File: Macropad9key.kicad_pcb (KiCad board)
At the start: 2 copper layers, 75 parts, among them J1 3220-10-0100-00, J2 4POS_2MM, J3 USB4085-GF-A, SW1 CherryMX_WithPCBPins, SW2 CherryMX_WithPCBPins, SW3 CherryMX_WithPCBPins, SW4 CherryMX_WithPCBPins, SW5 CherryMX_WithPCBPins, SW6 CherryMX_WithPCBPins, SW7 CherryMX_WithPCBPins, SW8 CherryMX_WithPCBPins, SW9 CherryMX_WithPCBPins, U1 ATSAMD11D14A-MUT, U2 MCP1700T-3302E-TT, U3 PCA9632DP2

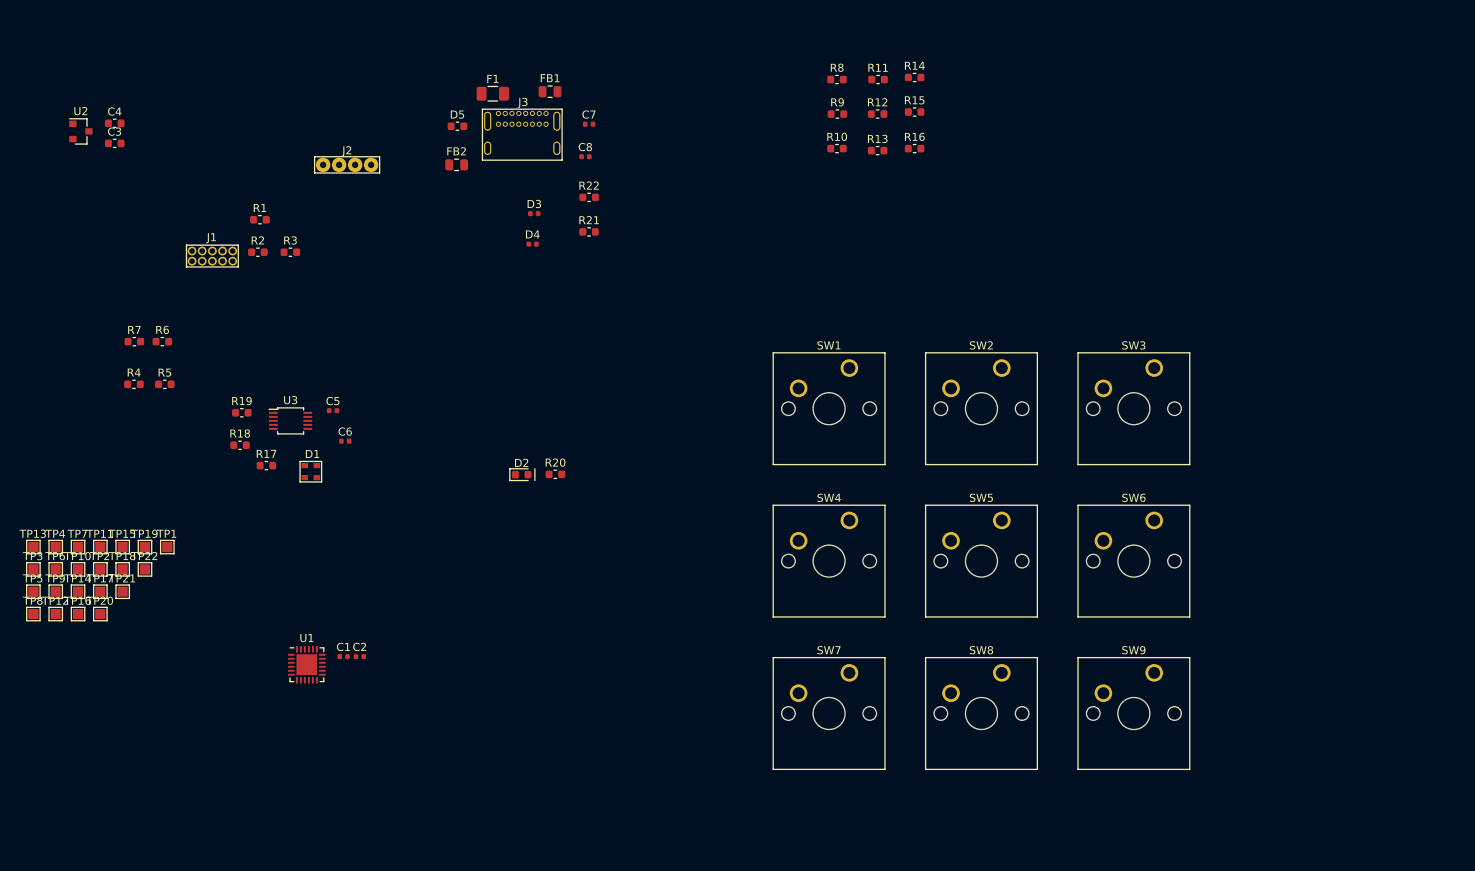
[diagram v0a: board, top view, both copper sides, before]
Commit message: Placed components, USB difference calc'd
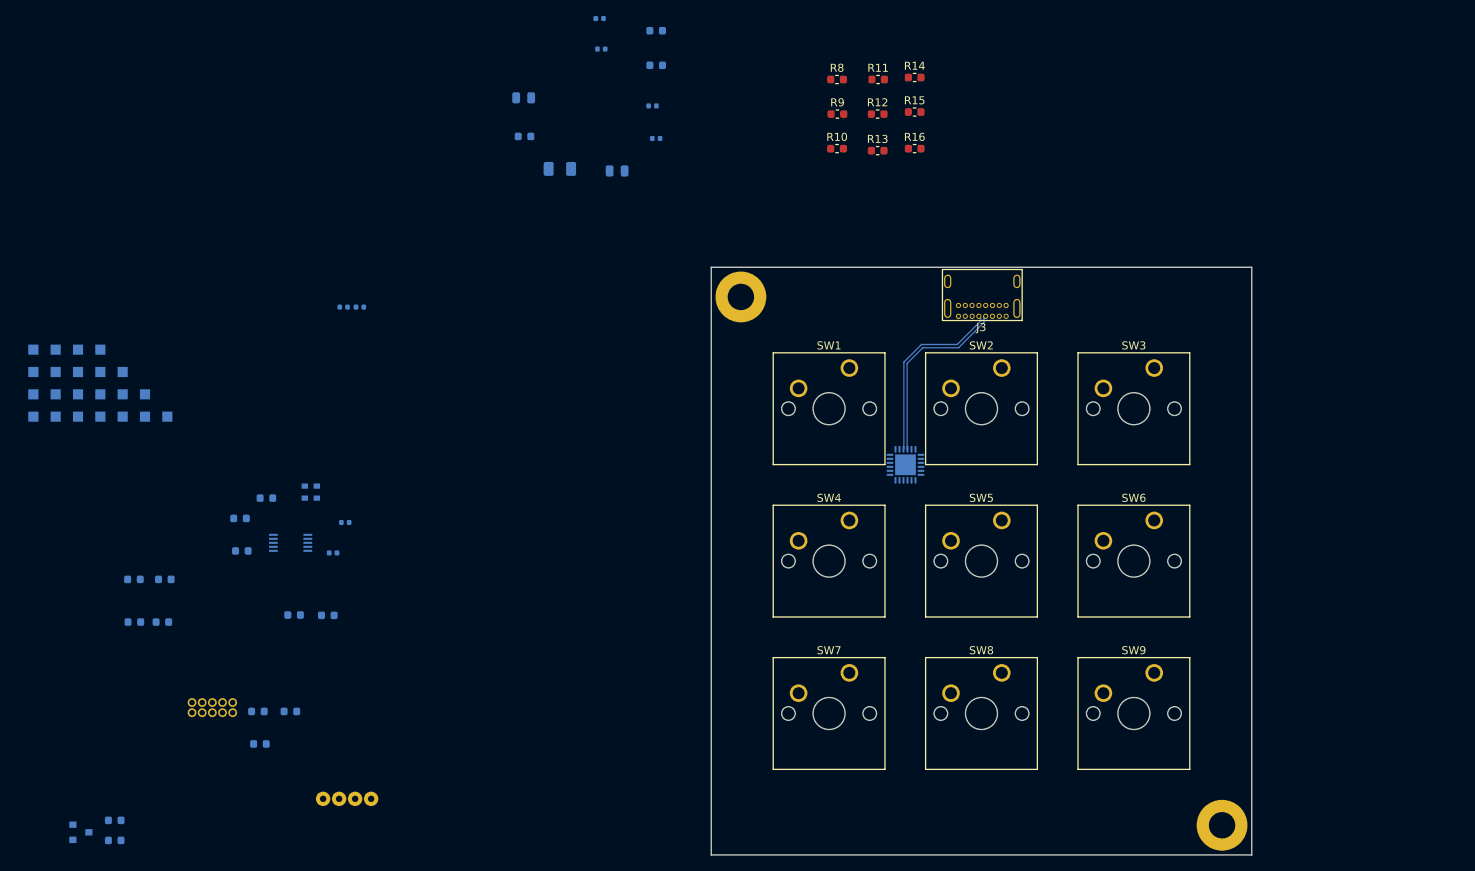
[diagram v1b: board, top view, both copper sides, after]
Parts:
- added REF**: 4-40_TypeF_MountingScrew, Zack_Mechanical:4-40_TypeF_MountingScrew, F.Cu at (206.1, 148.1)
- added REF**: 4-40_TypeF_MountingScrew, Zack_Mechanical:4-40_TypeF_MountingScrew, F.Cu at (145.9, 82.0)
- C1, C2, C3, C4, C5, C6, C7, C8, D1, D2, D3, D4, D5, F1, FB1, FB2, J1, J2, R1, R17, R18, R19, R2, R20, R21, R22, R3, R4, R5, R6, R7, TP1, TP10, TP11, TP12, TP13, TP14, TP15, TP16, TP17, TP18, TP19, TP2, TP20, TP21, TP22, TP3, TP4, TP5, TP6, TP7, TP8, TP9, U1, U2, U3: moved to B.Cu
- moved C4 89.6 mm to (67.7, 150.0)
- moved U2 87.6 mm to (63.4, 149.0)
- moved C3 84.6 mm to (67.7, 147.5)
- moved J2 79.2 mm to (96.7, 144.8)
- moved U1 78.9 mm to (166.5, 103.0), turned to 180 degrees
- moved R1 65.5 mm to (85.8, 137.9)
- moved J3 61.8 mm to (176.1, 83.1), turned to 180 degrees
- moved R2 57.4 mm to (85.6, 133.9)
- moved R3 57.4 mm to (89.6, 133.9)
- moved J1 53.8 mm to (76.7, 132.1)
- moved C1 43.7 mm to (96.3, 83.3)
- moved C2 43.7 mm to (98.3, 83.3)
- moved R6 35.1 mm to (73.6, 122.7)
- moved R7 35.1 mm to (70.1, 122.7)
- moved R20 33.5 mm to (94.3, 121.8)
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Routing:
- net USB_DP: track 0.00 -> 23.5 mm
- net USB_DN: track 0.00 -> 23.5 mm
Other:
- board outline added: 67.6 x 73.5 mm
- copper layers 2 -> 4

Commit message: Initial layout complete. Pins moved to make layout easy
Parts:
- added REF**: 4-40_TypeF_MountingScrew, Zack_Mechanical:4-40_TypeF_MountingScrew, F.Cu at (146.1, 148.0)
- added REF**: 4-40_TypeF_MountingScrew, Zack_Mechanical:4-40_TypeF_MountingScrew, F.Cu at (206.0, 82.1)
- R10, R11, R12, R13, R14, R15, R16, R8, R9: moved to B.Cu
- moved TP3 133.7 mm to (190.5, 81.3)
- moved TP2 132.7 mm to (198.1, 83.8)
- moved U2 130.9 mm to (184.2, 98.4), turned to 90 degrees
- moved TP16 130.0 mm to (193.0, 86.4)
- moved C3 128.2 mm to (187.0, 100.6), turned to 270 degrees
- moved TP22 127.8 mm to (195.5, 124.5)
- moved C4 126.3 mm to (184.3, 101.4)
- moved TP19 122.0 mm to (193.0, 106.7)
- moved TP8 110.3 mm to (167.6, 83.8)
- moved TP21 109.2 mm to (172.7, 124.5)
- moved TP18 107.6 mm to (175.2, 109.2)
- moved TP15 106.8 mm to (175.3, 91.4)
- moved TP1 106.1 mm to (180.3, 94.0)
- moved TP6 106.1 mm to (162.6, 122.1), turned to 90 degrees
- moved TP13 105.6 mm to (162.7, 105.4)
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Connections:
- C3 pad 1: Vbus -> VBus
- F1 pad 1: VBus -> Net-(C7-Pad1)
- F1 pad 2: Net-(C7-Pad1) -> Net-(D5-Pad1)
- FB1 pad 1: Net-(D5-Pad1) -> Net-(C7-Pad1)
- FB1 pad 2: Net-(C7-Pad1) -> VBus
- TP1 pad 1: Vbus -> VBus
- U1 pad 1: BUTTON1 -> BUTTON2
- U1 pad 10: TEST_IO1 -> BUTTON4
- U1 pad 11: ONBOARD_LED -> I2C_SDA
- U1 pad 12: TEST_IO2 -> I2C_SCL
- U1 pad 13: UART_TX -> TEST_IO2
- U1 pad 14: UART_RX -> TEST_IO1
- U1 pad 15: I2C_SCL -> Net-(U1-Pad15)
- U1 pad 16: I2C_SDA -> BUTTON1
- U1 pad 17: Net-(U1-Pad17) -> ONBOARD_LED
- U1 pad 2: BUTTON2 -> BUTTON3
- U1 pad 3: BUTTON3 -> BUTTON6
- U1 pad 4: BUTTON4 -> BUTTON9
- U1 pad 6: BUTTON6 -> BUTTON8
- U1 pad 7: BUTTON7 -> UART_TX
- U1 pad 8: BUTTON8 -> UART_RX
- U1 pad 9: BUTTON9 -> BUTTON7
- U2 pad 3: Vbus -> VBus
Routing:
- net GND: track 0.00 -> 66.1 mm, vias 0 -> 13
- net BUTTON9: track 0.00 -> 57.0 mm
- net BUTTON3: track 0.00 -> 45.5 mm
- net BUTTON7: track 0.00 -> 42.8 mm
- net SWCLK: track 0.00 -> 41.8 mm
- net BUTTON8: track 0.00 -> 40.6 mm
- net BUTTON6: track 0.00 -> 36.3 mm
- net I2C_SDA: track 0.00 -> 35.7 mm
- net SWRST: track 0.00 -> 34.5 mm, vias 0 -> 1
- net I2C_SCL: track 0.00 -> 33.0 mm
- net +3V3: track 0.00 -> 30.9 mm, vias 0 -> 10
- net BUTTON4: track 0.00 -> 28.6 mm
- net BUTTON1: track 0.00 -> 26.9 mm
- net SWDIO: track 0.00 -> 25.7 mm
- net Net-(D5-Pad1): track 0.00 -> 23.6 mm
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- added copper zone on B.Cu, net +3V3
- added copper zone on VCC, net +3V3
- added copper zone on GND, net GND

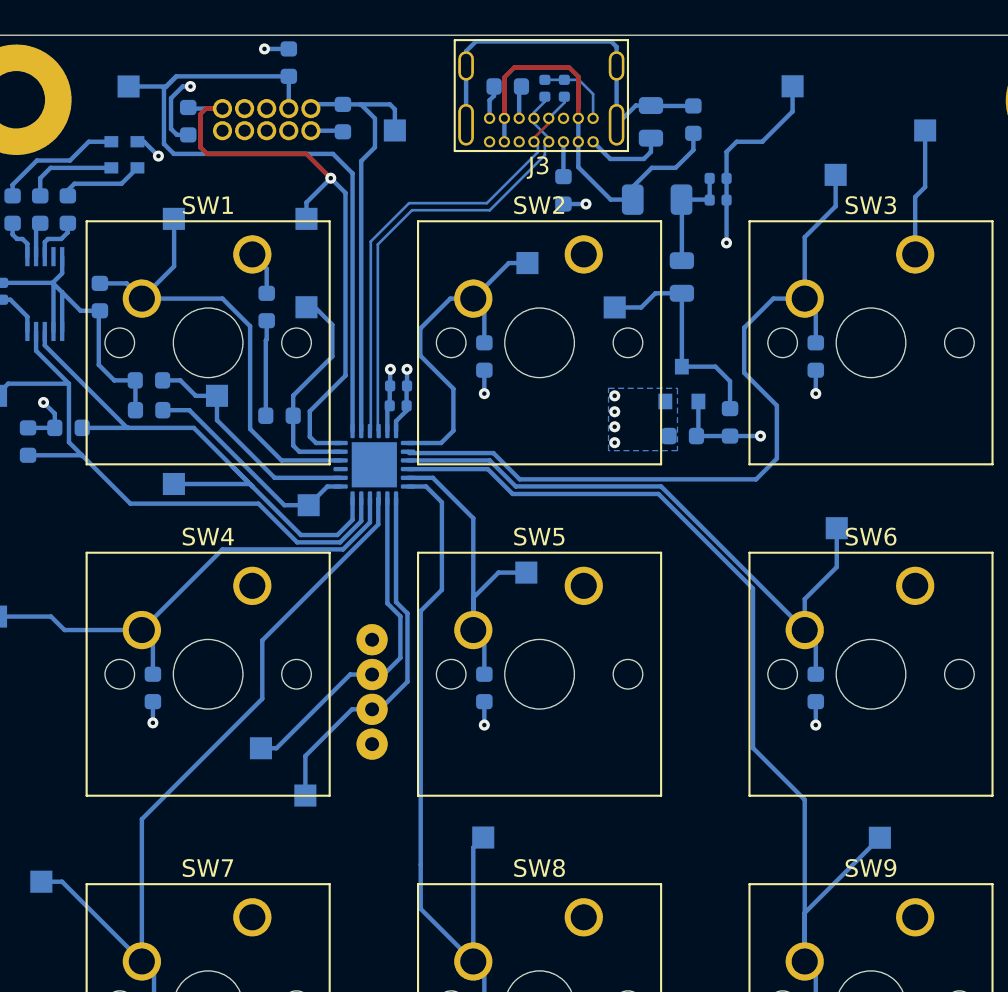
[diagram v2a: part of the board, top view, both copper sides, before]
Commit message: Silkscreen REFDES resized and aligned
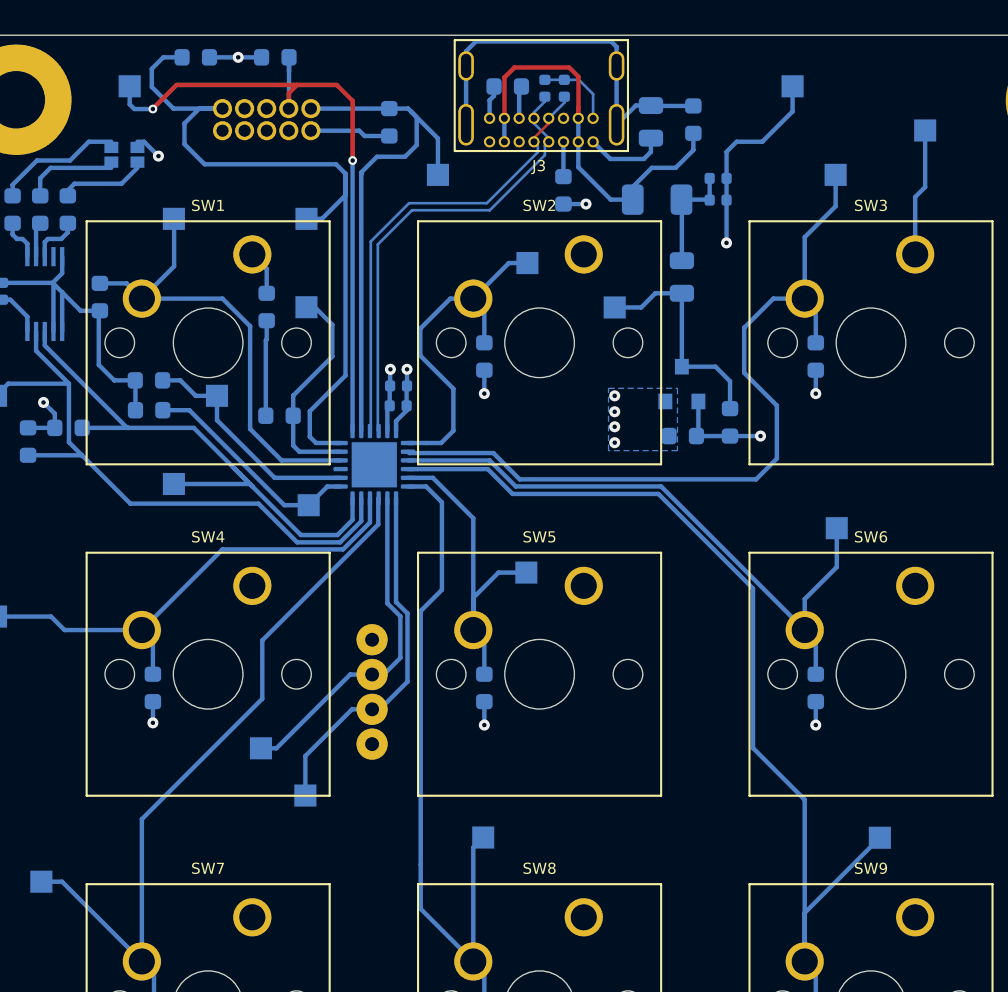
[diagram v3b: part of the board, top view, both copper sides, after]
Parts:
- F1: footprint Fuse:Fuse_1206_3216Metric -> Zack_Fuses:Fuse_1206_3216Metric
- moved R3 3.70 mm to (156.3, 79.6), turned to 180 degrees
- moved TP8 3.56 mm to (170.1, 86.4)
- moved R1 2.68 mm to (167.4, 83.3)
- moved R2 0.83 mm to (160.8, 79.6), turned to 0 degrees
- moved TP9 0.06 mm to (152.4, 81.3)
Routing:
- net SWRST: track 34.5 -> 43.3 mm, vias 1 -> 0
- net SWDIO: track 25.7 -> 30.9 mm
- net SWCLK: track 41.8 -> 39.3 mm, vias 0 -> 2
- net +3V3: track 30.9 -> 31.0 mm, vias 10 -> 9

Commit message: Adjust assembly layer. Add Fiducial Marks on SMD side
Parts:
- added REF**: Fiducial_1mm_Mask3mm, Fiducial:Fiducial_1mm_Mask3mm, B.Cu at (154.9, 144.8)
- added REF**: Fiducial_1mm_Mask3mm, Fiducial:Fiducial_1mm_Mask3mm, B.Cu at (205.7, 91.4)

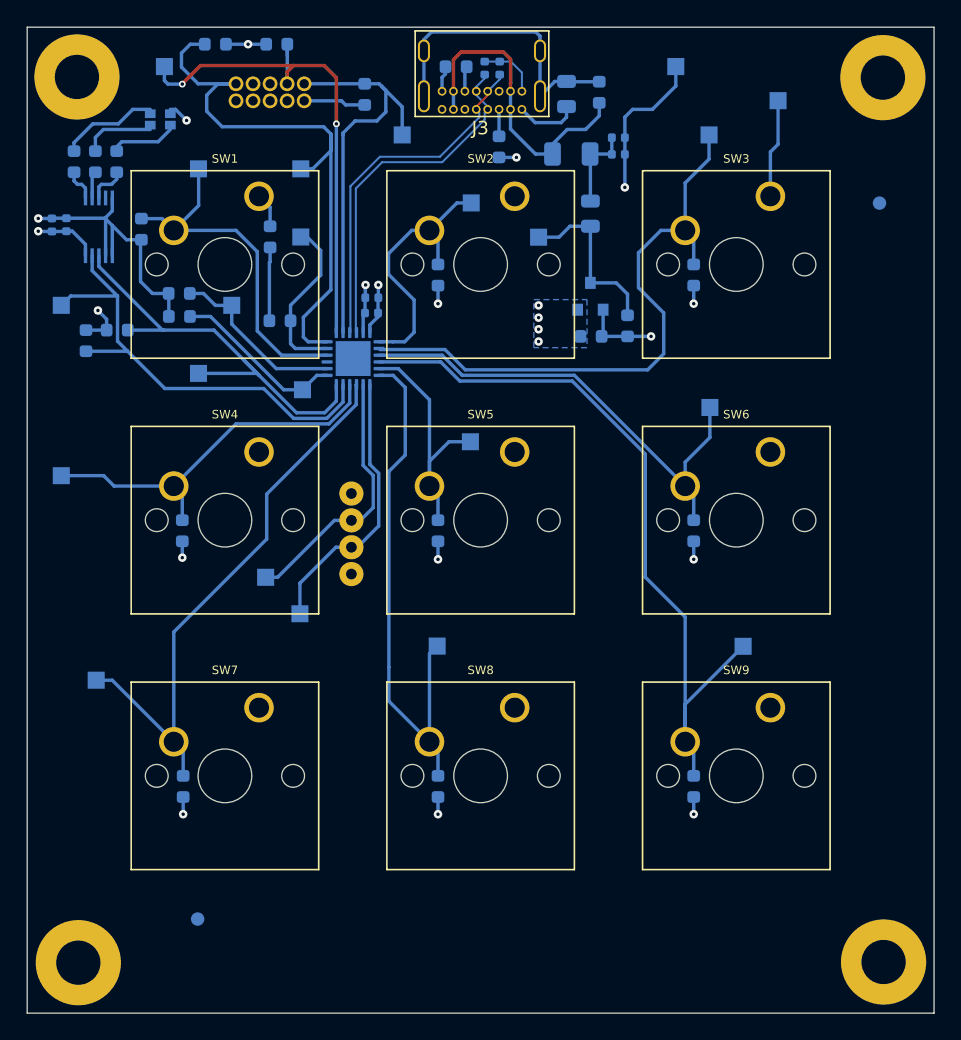
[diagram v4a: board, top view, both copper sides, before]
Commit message: Shrink PCB, move LED to opposite corner top side
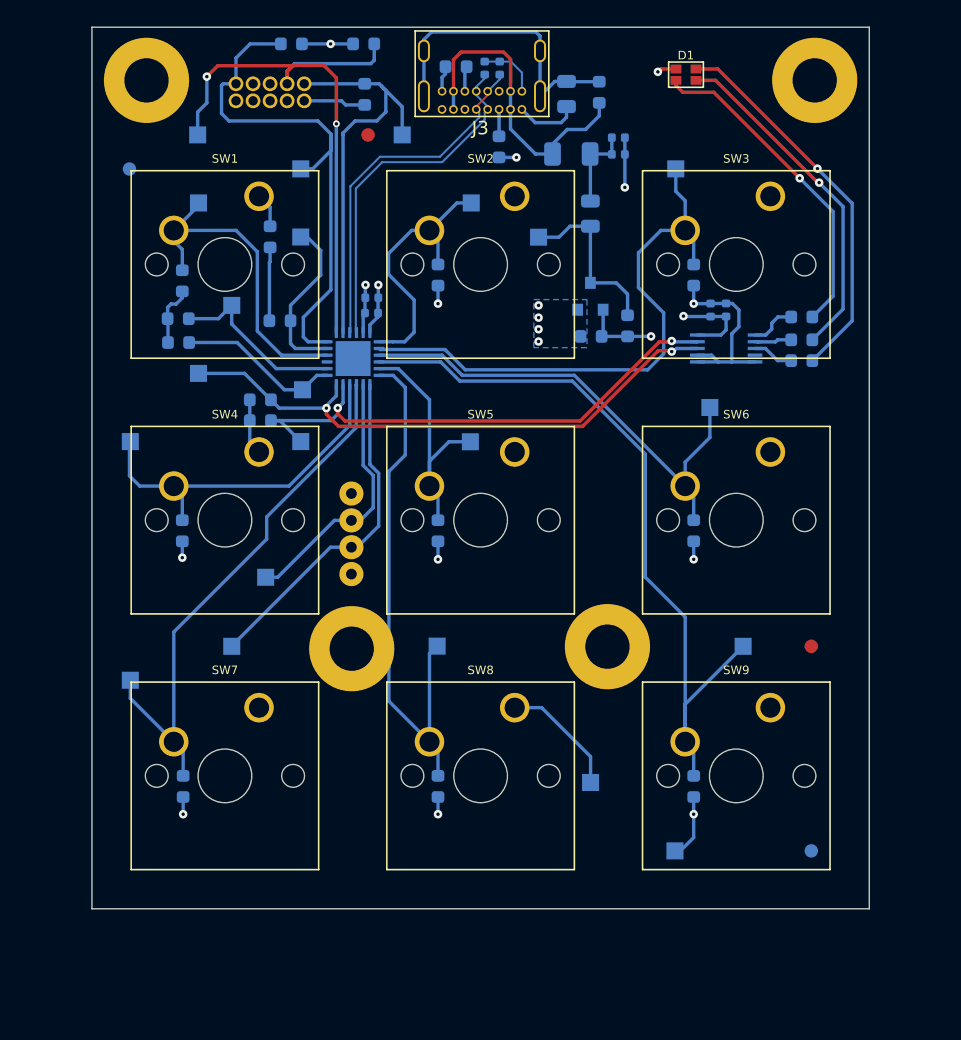
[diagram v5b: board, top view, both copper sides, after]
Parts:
- removed the REF** at (146.1, 148.0)
- removed the REF** at (206.0, 148.0)
- added REF**: 4-40_TypeF_MountingScrew, Zack_Mechanical:4-40_TypeF_MountingScrew, F.Cu at (185.5, 124.5)
- added REF**: 4-40_TypeF_MountingScrew, Zack_Mechanical:4-40_TypeF_MountingScrew, F.Cu at (166.4, 124.6)
- added REF**: Fiducial_1mm_Mask3mm, Fiducial:Fiducial_1mm_Mask3mm, F.Cu at (167.6, 86.4)
- added REF**: Fiducial_1mm_Mask3mm, Fiducial:Fiducial_1mm_Mask3mm, B.Cu at (149.9, 88.9)
- D1, REF**: moved to F.Cu
- moved TP3 58.4 mm to (190.4, 139.7)
- moved R19 56.2 mm to (199.9, 103.2), turned to 180 degrees
- moved R18 54.3 mm to (199.9, 101.6), turned to 0 degrees
- moved TP2 52.7 mm to (184.2, 134.6)
- moved R17 52.3 mm to (199.9, 99.9), turned to 0 degrees
- moved C5 50.6 mm to (194.3, 99.4)
- moved C6 48.4 mm to (193.2, 99.4)
- moved U3 47.6 mm to (194.3, 102.3), turned to 180 degrees
- moved REF** 46.0 mm to (200.7, 139.7)
- moved D1 39.3 mm to (191.3, 81.9), turned to 0 degrees
- moved REF** 33.4 mm to (200.7, 124.5)
- moved TP4 20.5 mm to (162.6, 109.2)
- moved R7 14.3 mm to (159.6, 107.6), turned to 0 degrees
- moved R6 11.9 mm to (159.6, 106.1)
- moved R2 6.48 mm to (167.3, 79.6)
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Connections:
- U3 pad 1: Net-(R19-Pad2) -> Net-(R17-Pad1)
- U3 pad 3: Net-(R17-Pad1) -> Net-(R19-Pad2)
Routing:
- net Net-(D1-Pad2): track 7.34 -> 28.7 mm, vias 0 -> 1
- net Net-(D1-Pad4): track 5.35 -> 25.7 mm, vias 0 -> 1
- net Net-(D1-Pad3): track 4.85 -> 24.5 mm, vias 0 -> 1
- net I2C_SCL: track 33.0 -> 43.6 mm, vias 0 -> 2
- net GND: track 66.1 -> 57.7 mm, vias 13 -> 12
- net SWCLK: track 39.3 -> 44.5 mm
- net +3V3: track 31.0 -> 36.0 mm, vias 9 -> 8
- net UART_TX: track 20.7 -> 25.5 mm
- net I2C_SDA: track 35.7 -> 40.3 mm, vias 0 -> 2
- net SWRST: track 43.3 -> 39.6 mm
- net BUTTON3: track 45.5 -> 42.5 mm
- net BUTTON1: track 26.9 -> 24.8 mm
- net BUTTON7: track 42.8 -> 41.0 mm
- net BUTTON4: track 28.6 -> 27.0 mm
- net Net-(R18-Pad1): track 2.02 -> 2.76 mm
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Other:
- board size 67.6 x 73.5 mm -> 57.9 x 65.7 mm
